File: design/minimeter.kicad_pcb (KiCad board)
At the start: 2 copper layers, 4 parts

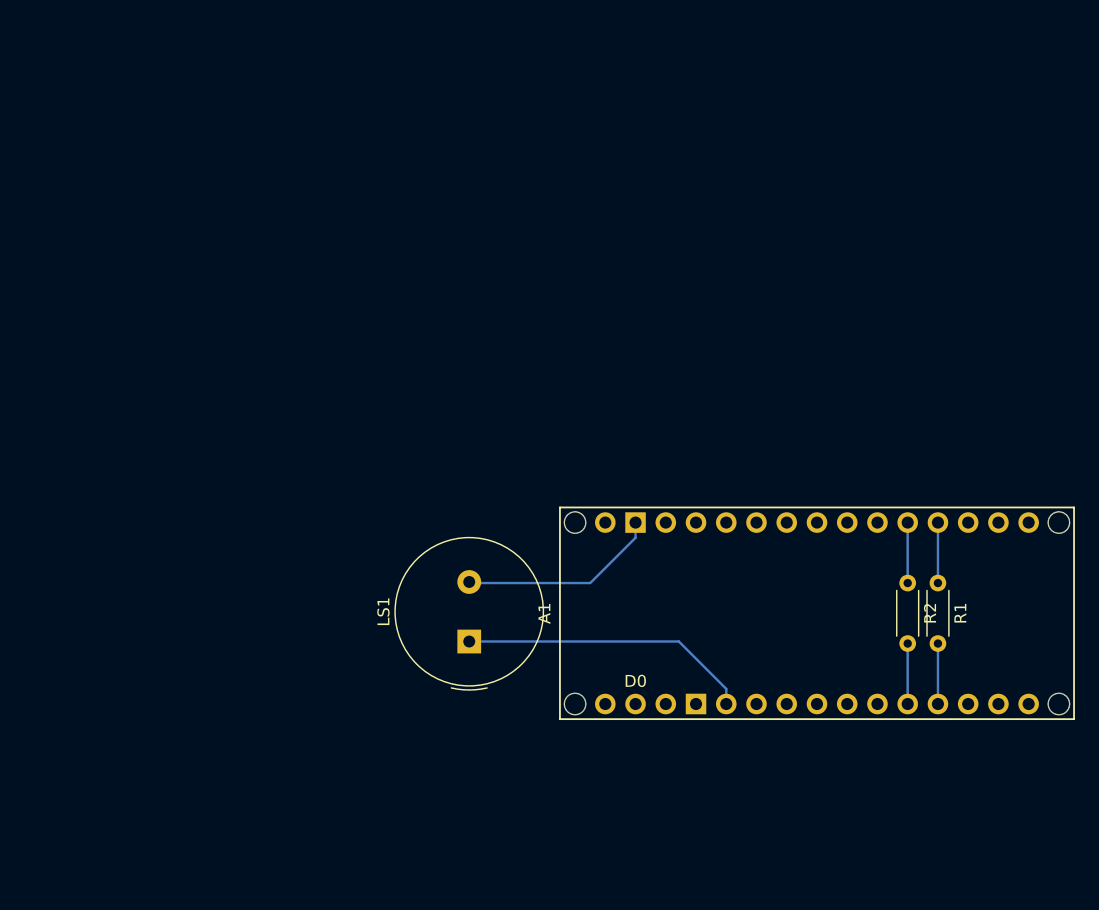
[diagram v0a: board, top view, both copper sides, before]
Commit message: Fix design PCB footprints of components
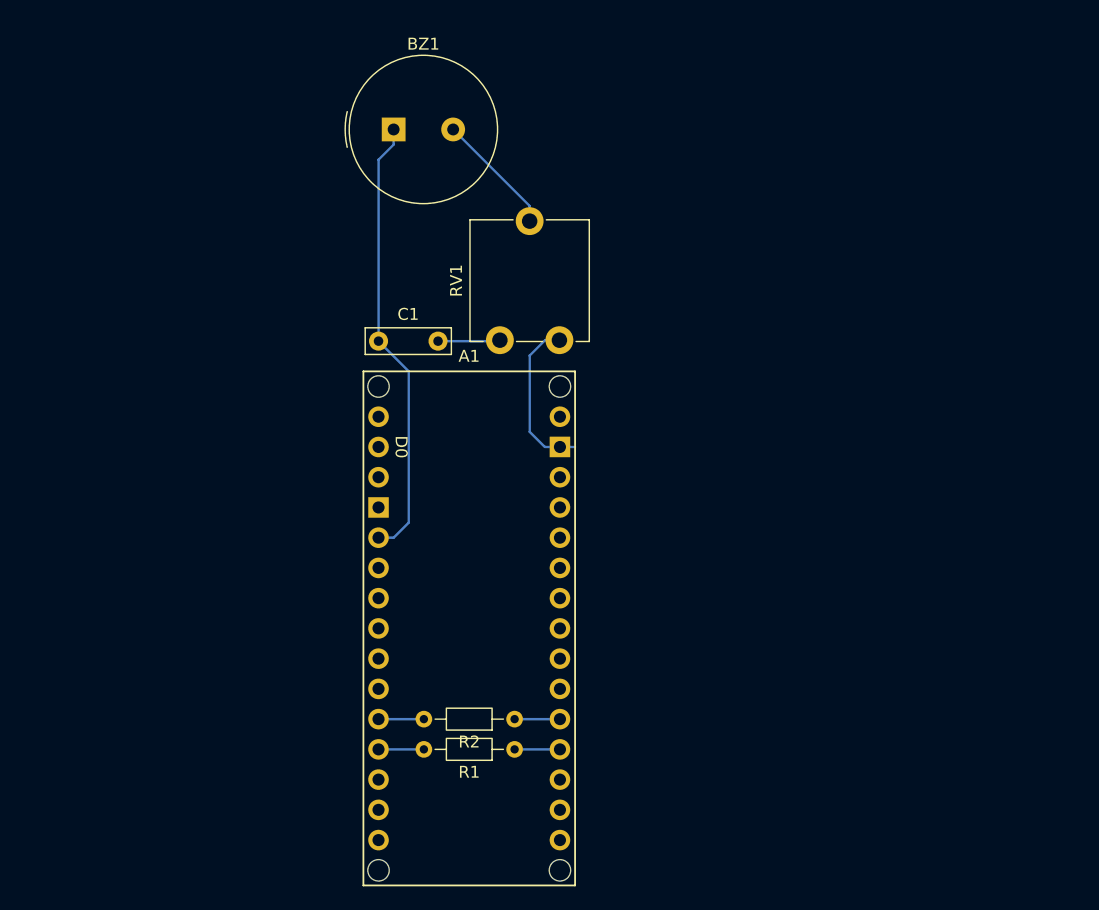
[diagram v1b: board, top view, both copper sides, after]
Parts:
- removed LS1: Speaker, Buzzer_Beeper:Buzzer_TDK_PS1240P02BT_D12.2mm_H6.5mm
- added BZ1: Buzzer, Buzzer_Beeper:Buzzer_TDK_PS1240P02BT_D12.2mm_H6.5mm, F.Cu at (63.5, 41.9)
- added C1: 100nF, Capacitor_THT:C_Rect_L7.0mm_W2.0mm_P5.00mm, F.Cu at (62.2, 59.7)
- added RV1: 100, Potentiometer_THT:Potentiometer_ACP_CA9-V10_Vertical, F.Cu at (77.4, 59.6)
- R1, R2: footprint Resistor_THT:R_Axial_DIN0204_L3.6mm_D1.6mm_P5.08mm_Horizontal -> Resistor_THT:R_Axial_DIN0204_L3.6mm_D1.6mm_P7.62mm_Horizontal
- moved A1 55.7 mm to (69.8, 105.4), turned to 0 degrees
- moved R1 38.2 mm to (73.7, 94.0), turned to 180 degrees
- moved R2 34.9 mm to (73.7, 91.4), turned to 180 degrees
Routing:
- net Net-(A1-D2_INT0): track 24.5 -> 37.7 mm
- net Net-(BZ1--): track 0.00 -> 10.4 mm
- net Net-(C1-Pad2): track 0.00 -> 5.23 mm
- net GND: track 16.9 -> 13.8 mm
- net Net-(A1-PadA1): track 5.08 -> 3.81 mm
- net Net-(A1-PadA0): track 5.08 -> 3.81 mm
- net Net-(A1-PadD9): track 5.08 -> 3.81 mm
- net Net-(A1-PadD8): track 5.08 -> 3.81 mm

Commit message: Add switch and pin headers
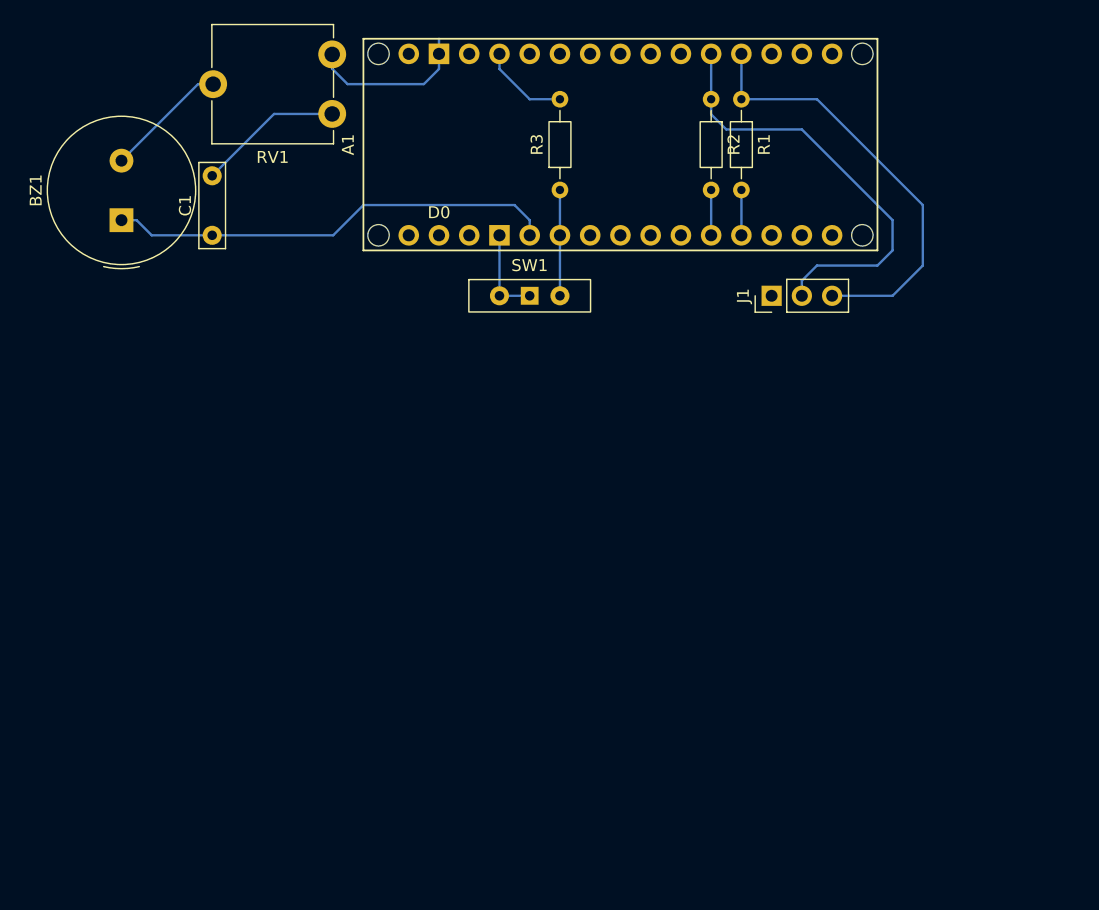
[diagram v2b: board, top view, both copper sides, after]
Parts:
- added J1: Conn_01x03_Pin, Connector_PinHeader_2.54mm:PinHeader_1x03_P2.54mm_Vertical, F.Cu at (95.2, 55.9)
- added R3: 1M, Resistor_THT:R_Axial_DIN0204_L3.6mm_D1.6mm_P7.62mm_Horizontal, F.Cu at (77.5, 47.0)
- added SW1: SW_SPDT, Button_Switch_THT:SW_Slide-03_Wuerth-WS-SLTV_10x2.5x6.4_P2.54mm, F.Cu at (74.9, 55.9)
- moved A1 71.1 mm to (104.1, 43.2), turned to 90 degrees
- moved R1 57.8 mm to (92.7, 39.4), turned to -90 degrees
- moved R2 54.6 mm to (90.2, 39.4), turned to -90 degrees
- moved RV1 30.7 mm to (58.3, 35.6), turned to 180 degrees
- moved BZ1 24.1 mm to (40.6, 49.5), turned to 90 degrees
- moved C1 16.6 mm to (48.3, 50.8), turned to 90 degrees
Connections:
- A1 pad D3: unconnected-(A1-D3_INT1-PadD3) -> Net-(A1-D3_INT1)
- A1 pad GND1: unconnected-(A1-GND-PadGND1) -> GND
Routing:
- net Net-(J1-Pin_3): track 3.81 -> 36.5 mm
- net Net-(J1-Pin_2): track 3.81 -> 36.5 mm
- net Net-(A1-D3_INT1): track 0.00 -> 8.89 mm
- net GND: track 13.8 -> 21.4 mm
- net VCC: track 0.00 -> 7.40 mm
- net Net-(C1-Pad2): track 5.23 -> 12.2 mm

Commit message: Implement continuity and voltmeter modes
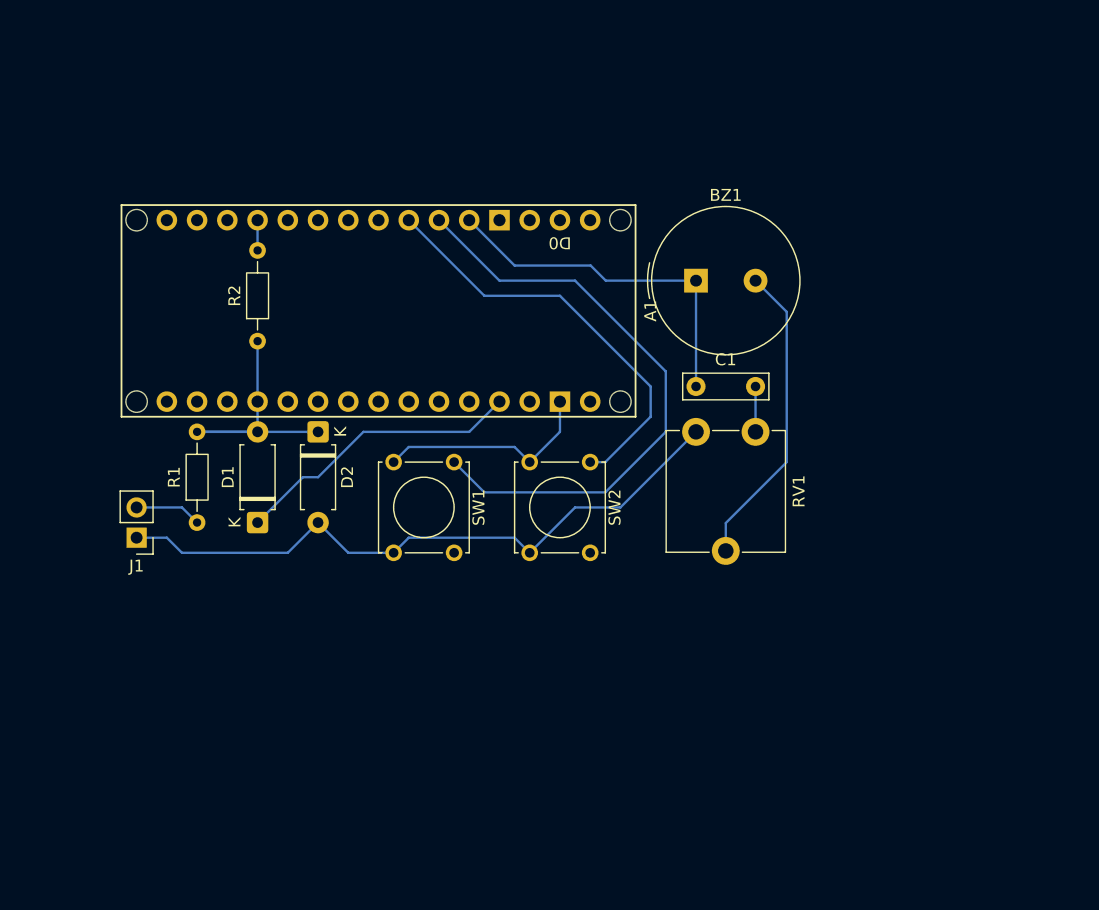
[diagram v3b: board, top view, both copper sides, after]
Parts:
- removed R3: 1M, Resistor_THT:R_Axial_DIN0204_L3.6mm_D1.6mm_P7.62mm_Horizontal
- added D1: D_Small_Filled, Diode_THT:D_A-405_P7.62mm_Horizontal, F.Cu at (52.1, 74.9)
- added D2: D_Small_Filled, Diode_THT:D_A-405_P7.62mm_Horizontal, F.Cu at (57.1, 67.3)
- added SW2: SW_Push_Dual, Button_Switch_THT:SW_Tactile_Straight_KSA0Axx1LFTR, F.Cu at (80.0, 69.8)
- J1: value Conn_01x03_Pin -> Conn_01x02_Pin; footprint Connector_PinHeader_2.54mm:PinHeader_1x03_P2.54mm_Vertical -> Connector_PinHeader_2.54mm:PinHeader_1x02_P2.54mm_Vertical
- R1, R2: value 1M -> 10K
- SW1: value SW_SPDT -> SW_Push_Dual; footprint Button_Switch_THT:SW_Slide-03_Wuerth-WS-SLTV_10x2.5x6.4_P2.54mm -> Button_Switch_THT:SW_Tactile_Straight_KSA0Axx1LFTR
- moved A1 65.0 mm to (40.6, 57.1), turned to -90 degrees
- moved R1 57.9 mm to (47.0, 74.9), turned to 90 degrees
- moved J1 57.1 mm to (41.9, 76.2), turned to 180 degrees
- moved BZ1 48.5 mm to (88.9, 54.6), turned to 0 degrees
- moved RV1 44.0 mm to (88.9, 67.3), turned to -90 degrees
- moved R2 43.2 mm to (52.1, 59.7), turned to 90 degrees
- moved C1 42.6 mm to (88.9, 63.5), turned to 0 degrees
- moved SW1 15.3 mm to (68.6, 69.8), turned to -90 degrees
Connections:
- A1 pad A0: Net-(J1-Pin_3) -> Net-(D1-A)
- A1 pad A1: Net-(J1-Pin_2) -> unconnected-(A1-PadA1)
- A1 pad D4: unconnected-(A1-PadD4) -> Net-(A1-PadD4)
- A1 pad D8: Net-(A1-PadD8) -> unconnected-(A1-PadD8)
- R1 pad 1: Net-(J1-Pin_3) -> Net-(J1-Pin_2)
- R1 pad 2: Net-(A1-PadD9) -> Net-(D1-A)
- R2 pad 1: Net-(J1-Pin_2) -> Net-(D1-A)
- R2 pad 2: Net-(A1-PadD8) -> Net-(A1-PadD9)
- SW1 pad 1: GND -> Net-(A1-D3_INT1)
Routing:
- net GND: track 21.4 -> 73.6 mm
- net Net-(A1-D3_INT1): track 8.89 -> 50.3 mm
- net Net-(J1-Pin_3): track 36.5 -> 0.00 mm
- net Net-(A1-PadD4): track 0.00 -> 35.3 mm
- net Net-(J1-Pin_2): track 36.5 -> 5.61 mm
- net Net-(D1-A): track 0.00 -> 22.9 mm
- net VCC: track 7.40 -> 24.5 mm
- net Net-(BZ1--): track 10.4 -> 25.9 mm
- net Net-(C1-Pad2): track 12.2 -> 3.81 mm
- net Net-(A1-D2_INT0): track 37.7 -> 30.0 mm
- net Net-(A1-PadD8): track 3.81 -> 0.00 mm
- net Net-(A1-PadD9): track 3.81 -> 2.54 mm

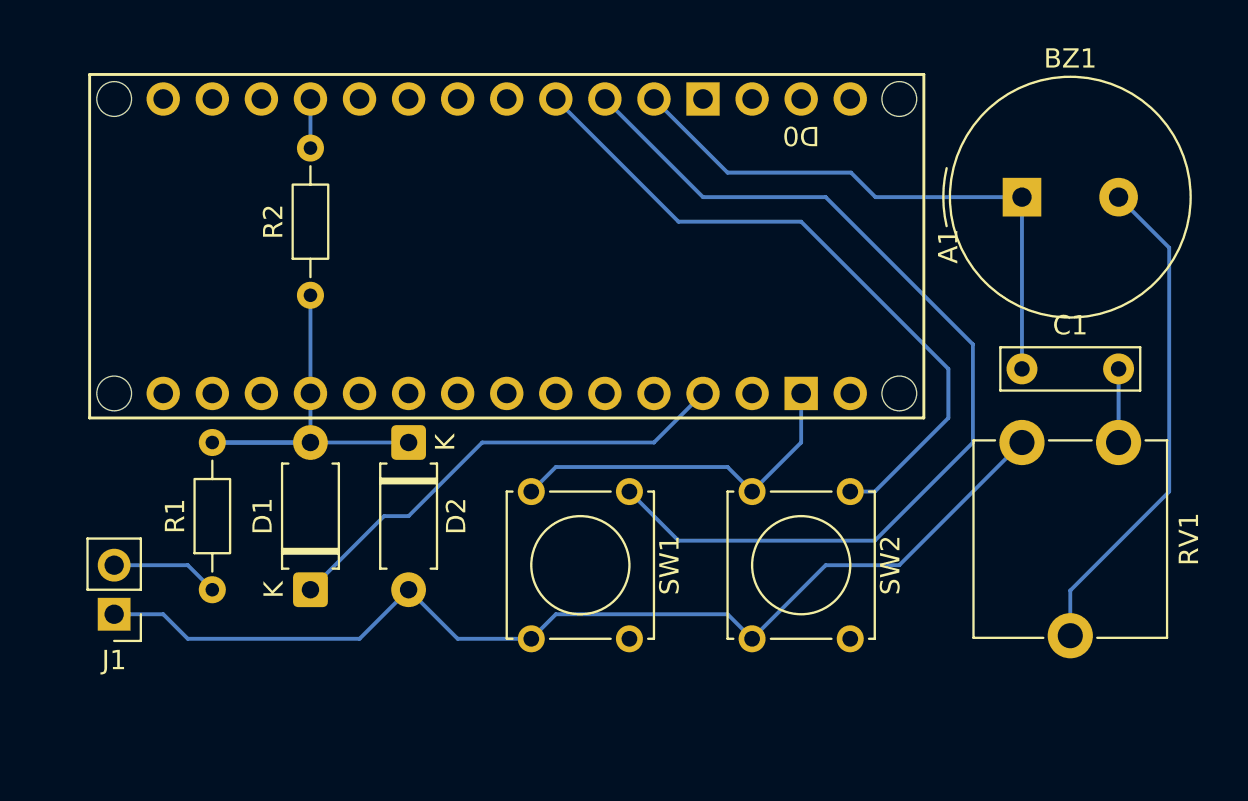
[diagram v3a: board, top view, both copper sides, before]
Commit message: Update button configuration and PCB layout
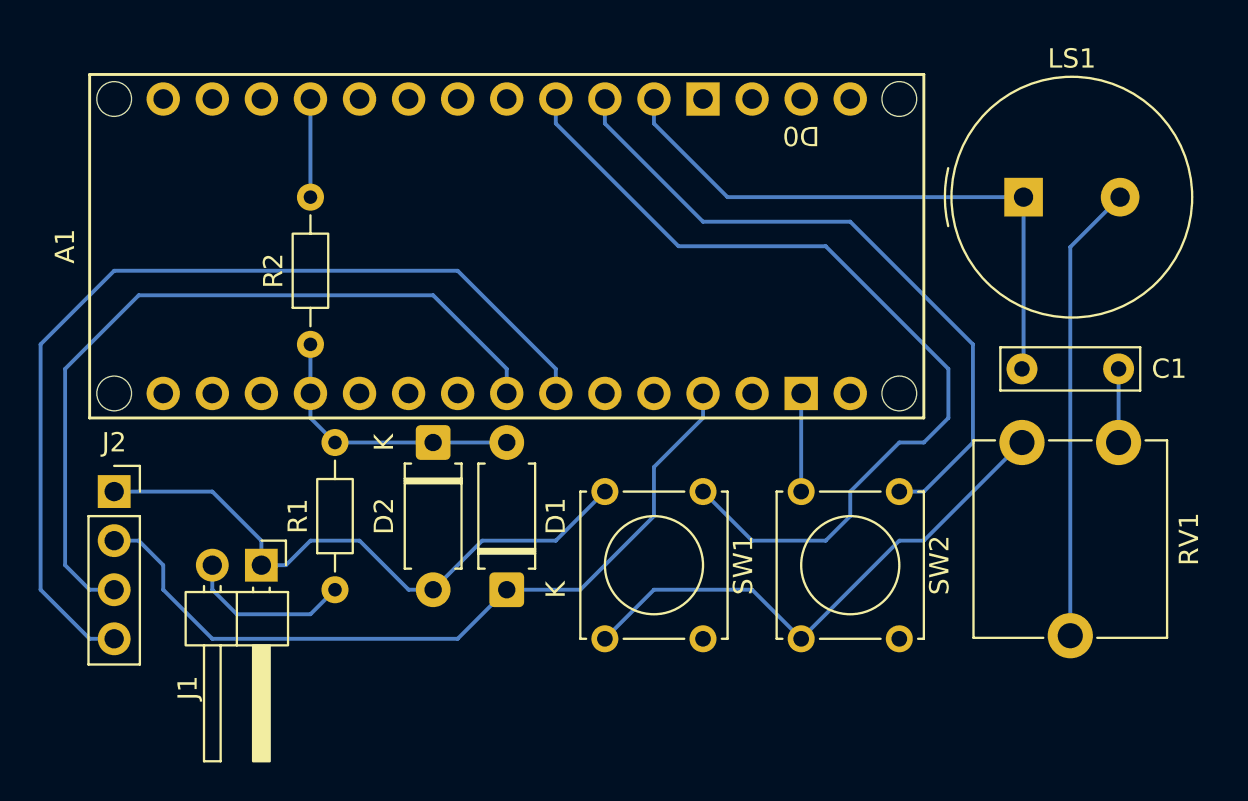
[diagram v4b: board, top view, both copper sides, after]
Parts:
- removed BZ1: Buzzer, Buzzer_Beeper:Buzzer_TDK_PS1240P02BT_D12.2mm_H6.5mm
- added J2: I2C, Connector_PinSocket_2.54mm:PinSocket_1x04_P2.54mm_Vertical, F.Cu at (41.9, 69.8)
- added LS1: Speaker, Buzzer_Beeper:Buzzer_TDK_PS1240P02BT_D12.2mm_H6.5mm, F.Cu at (89.0, 54.6)
- J1: footprint Connector_PinHeader_2.54mm:PinHeader_1x02_P2.54mm_Vertical -> Connector_PinHeader_2.54mm:PinHeader_1x02_P2.54mm_Horizontal
- RV1: value 100 -> 10K
- moved D1 10.2 mm to (62.2, 74.9)
- moved J1 8.03 mm to (49.5, 73.7), turned to -90 degrees
- moved R1 6.35 mm to (53.3, 74.9)
- moved SW1 3.81 mm to (72.4, 69.8)
- moved R2 2.54 mm to (52.1, 62.2)
- moved SW2 2.54 mm to (82.5, 69.8)
- moved D2 1.27 mm to (58.4, 67.3)
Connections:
- net Net-(A1-D2_INT0) renamed /SPKR
- net Net-(A1-PadD9) renamed /PULL
- net Net-(D1-A) renamed /IN_PROT
- net Net-(J1-Pin_2) renamed /IN
- A1 pad A4: unconnected-(A1-A4/SDA-PadA4) -> /SDA
- A1 pad A5: unconnected-(A1-A5/SCL-PadA5) -> /SCL
- A1 pad D3: Net-(A1-D3_INT1) -> /BTN_2
- A1 pad D4: Net-(A1-PadD4) -> /BTN_1
- SW1 pad 1: Net-(A1-D3_INT1) -> /BTN_1
- SW2 pad 1: Net-(A1-PadD4) -> /BTN_2
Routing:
- net Net-(A1-D3_INT1): track 50.3 -> 0.00 mm
- net /SCL: track 0.00 -> 49.2 mm
- net /BTN_1: track 0.00 -> 46.5 mm
- net /SDA: track 0.00 -> 40.5 mm
- net Net-(A1-PadD4): track 35.3 -> 0.00 mm
- net /BTN_2: track 0.00 -> 35.0 mm
- net VCC: track 24.5 -> 40.8 mm
- net GND: track 73.6 -> 64.4 mm
- net /IN_PROT: track 22.9 -> 14.5 mm
- net /IN: track 5.61 -> 8.67 mm
- net /PULL: track 2.54 -> 5.08 mm
- net Net-(LS1-Pad2): track 25.9 -> 23.8 mm
- net /SPKR: track 30.0 -> 30.9 mm

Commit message: Iterate on PCB
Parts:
- R1, R2: footprint Resistor_THT:R_Axial_DIN0204_L3.6mm_D1.6mm_P7.62mm_Horizontal -> Resistor_THT:R_Axial_DIN0207_L6.3mm_D2.5mm_P7.62mm_Horizontal
- moved A1 49.5 mm to (90.2, 57.1), turned to 90 degrees
- moved D2 31.8 mm to (86.4, 52.1)
- moved R2 28.5 mm to (78.7, 52.1), turned to -90 degrees
- moved R1 26.4 mm to (74.9, 59.7)
- moved D1 25.4 mm to (82.5, 59.7)
- moved C1 25.0 mm to (64.8, 69.8), turned to -90 degrees
- moved SW1 22.9 mm to (49.5, 68.6)
- moved SW2 21.6 mm to (61.0, 68.6)
- moved RV1 21.5 mm to (68.7, 74.9), turned to 0 degrees
- moved J2 20.5 mm to (44.5, 49.5)
- moved LS1 16.6 mm to (88.9, 71.2), turned to -90 degrees
- moved J1 10.2 mm to (44.5, 64.8), turned to 180 degrees
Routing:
- net GND: track 64.4 -> 0.00 mm
- net VCC: track 40.8 -> 0.00 mm
- net /SCL: track 49.2 -> 25.5 mm
- net /IN: track 8.67 -> 31.5 mm
- net /BTN_2: track 35.0 -> 12.5 mm
- net /BTN_1: track 46.5 -> 28.6 mm
- net /SDA: track 40.5 -> 27.0 mm
- net Net-(LS1-Pad2): track 23.8 -> 11.7 mm
- net Net-(C1-Pad2): track 3.81 -> 6.61 mm
- net /SPKR: track 30.9 -> 33.4 mm
- net /IN_PROT: track 14.5 -> 14.0 mm
- added copper zone on F.Cu, net GND
- added copper zone on B.Cu, net VCC
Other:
- board outline added: 49.5 x 31.7 mm
- board text added: "MiniMeter v1 2026-01-16 Jasmine Tai"
- board text added: "USB Side"

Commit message: Iterate on PCB again
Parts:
- A1, C1, D1, D2, R1, R2: moved to B.Cu
- J2: footprint Connector_PinSocket_2.54mm:PinSocket_1x04_P2.54mm_Vertical -> Connector_PinSocket_2.54mm:PinSocket_1x04_P2.54mm_Horizontal; moved to B.Cu
- moved A1 44.5 mm to (45.7, 57.1)
- moved J2 40.8 mm to (85.1, 53.3), turned to 180 degrees
- moved D1 26.7 mm to (55.9, 59.7)
- moved D2 24.1 mm to (62.2, 52.1)
- moved R1 22.2 mm to (52.7, 59.7)
- moved R2 19.7 mm to (59.1, 52.1)
- moved C1 14.2 mm to (71.0, 57.1), turned to 180 degrees
- moved LS1 13.8 mm to (81.3, 59.7), turned to 90 degrees
- moved RV1 13.0 mm to (71.1, 62.1), turned to 90 degrees
- moved SW2 11.5 mm to (72.4, 67.3), turned to 0 degrees
- moved J1 8.13 mm to (49.5, 58.4)
- moved SW1 5.24 mm to (54.6, 67.3), turned to 0 degrees
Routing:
- net /IN: track 31.5 -> 5.87 mm
- net /SPKR: track 33.4 -> 20.5 mm
- net /BTN_1: track 28.6 -> 17.0 mm
- net /SDA: track 27.0 -> 31.8 mm
- net /SCL: track 25.5 -> 22.0 mm
- net /BTN_2: track 12.5 -> 10.2 mm
- net Net-(LS1-Pad2): track 11.7 -> 13.8 mm
- net Net-(C1-Pad2): track 6.61 -> 4.98 mm
- net /IN_PROT: track 14.0 -> 12.6 mm
- net /PULL: track 5.08 -> 5.87 mm
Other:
- board size 49.5 x 31.7 mm -> 44.4 x 26.7 mm
- board text added: "+"
- board text added: "-"
- board text added: "Copyright © 2026 Jasmine Tai. All rights reserved."
- board text added: "MODE"
- board text added: "MiniMeter v1 2026-01-17 Jasmine Tai"
- board text added: "OK"
- board text added: "USB SIDE"
- board text added: "VOLUME"
- board text added: "← I²C LCD"
- board text removed: "MiniMeter v1 2026-01-16 Jasmine Tai"
- board text removed: "USB Side"
